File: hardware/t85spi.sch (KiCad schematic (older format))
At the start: 12 parts, among them J1 AVRISP6, P1 Ethernet, SW1 SPST, U1 ATTINY85

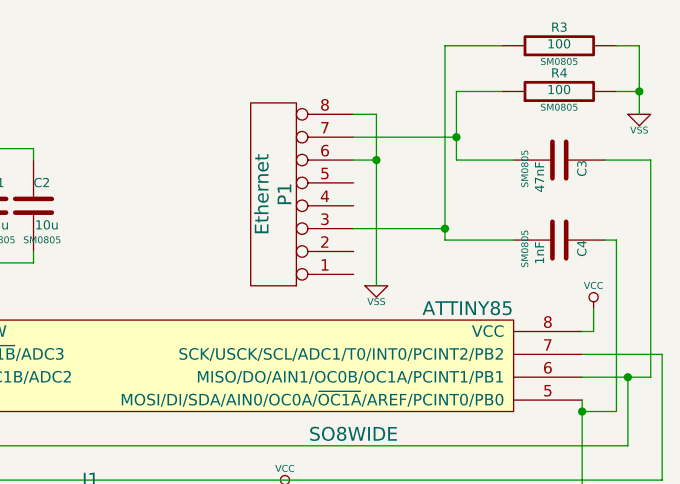
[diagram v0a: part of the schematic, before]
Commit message: fix orientation of pins
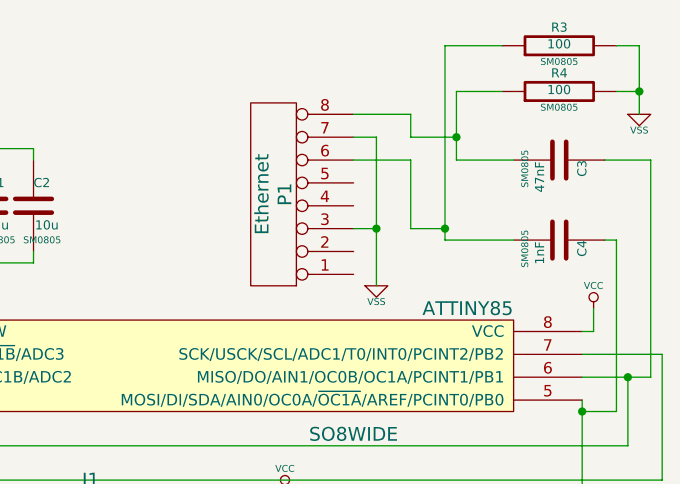
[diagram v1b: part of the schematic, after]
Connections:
- net VSS: now also P1.3 (P3), P1.7 (P7); no longer P1.6 (P6), P1.8 (P8)
- net at C3.2, R4.1: now also P1.8 (P8); no longer P1.7 (P7)
- net at C4.2, R3.1: now also P1.6 (P6); no longer P1.3 (P3)
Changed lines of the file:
@@
 Sheet 1 1
 Title ""
-Date "4 sep 2014"
+Date "5 sep 2014"
 Rev ""
 Comp ""
@@
 $EndComp
 Wire Wire Line
-	5400 1100 5400 1850
-Wire Wire Line
-	5300 1300 5400 1300
-Connection ~ 5400 1300
-Wire Wire Line
-	5300 1600 5700 1600
+	5300 1300 5550 1300
 Wire Wire Line
 	5700 800  5700 1650
@@
 	1    0    0    -1
 $EndComp
-Wire Wire Line
-	5400 1100 5300 1100
-Wire Wire Line
-	5300 1200 5750 1200
 Wire Wire Line
 	5750 1000 5750 1300
@@
 	5750 1000 5950 1000
 Connection ~ 5750 1200
+Wire Wire Line
+	5300 1100 5550 1100
+Wire Wire Line
+	5550 1100 5550 1200
+Wire Wire Line
+	5550 1200 5750 1200
+Wire Wire Line
+	5550 1300 5550 1600
+Wire Wire Line
+	5550 1600 5700 1600
+Wire Wire Line
+	5400 1200 5400 1850
+Wire Wire Line
+	5400 1600 5300 1600
+Wire Wire Line
+	5400 1200 5300 1200
+Connection ~ 5400 1600
 $EndSCHEMATC

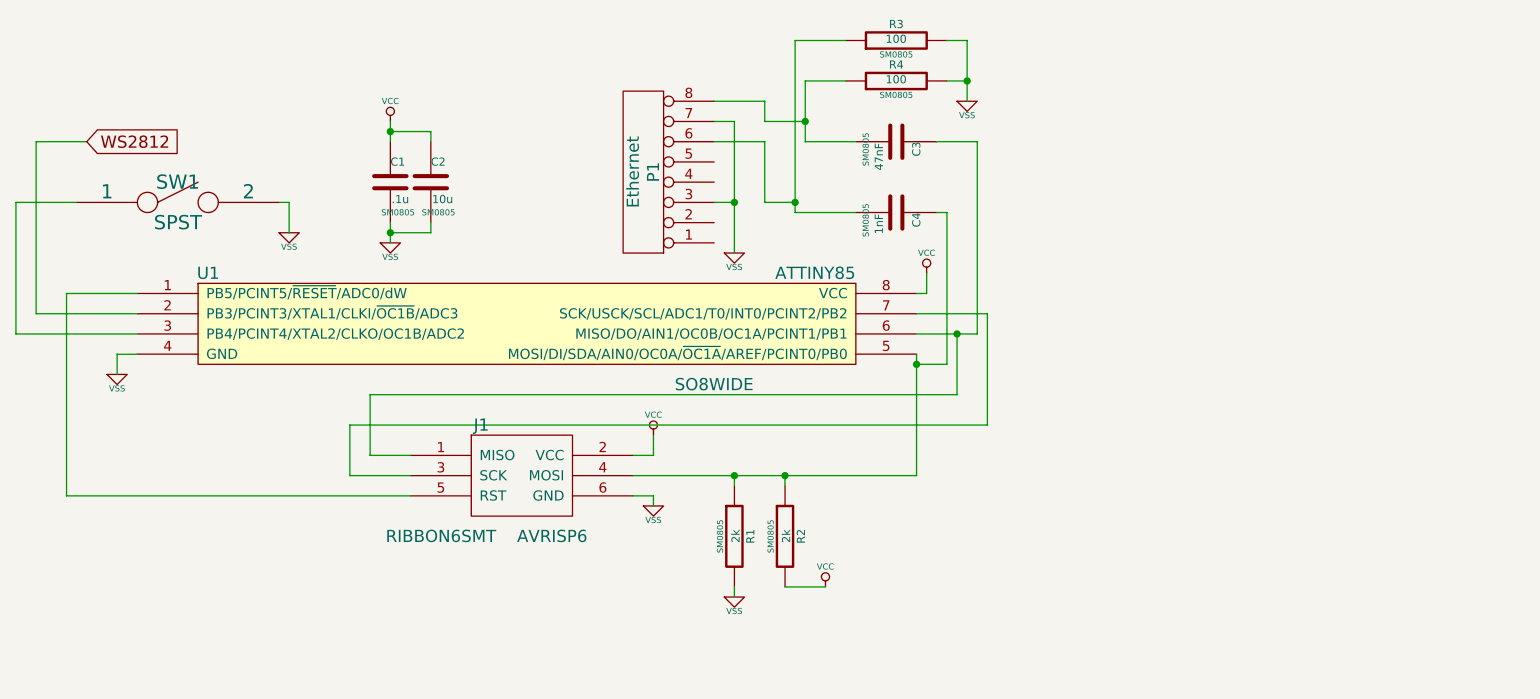
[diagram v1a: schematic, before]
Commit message: add documentation + warnings
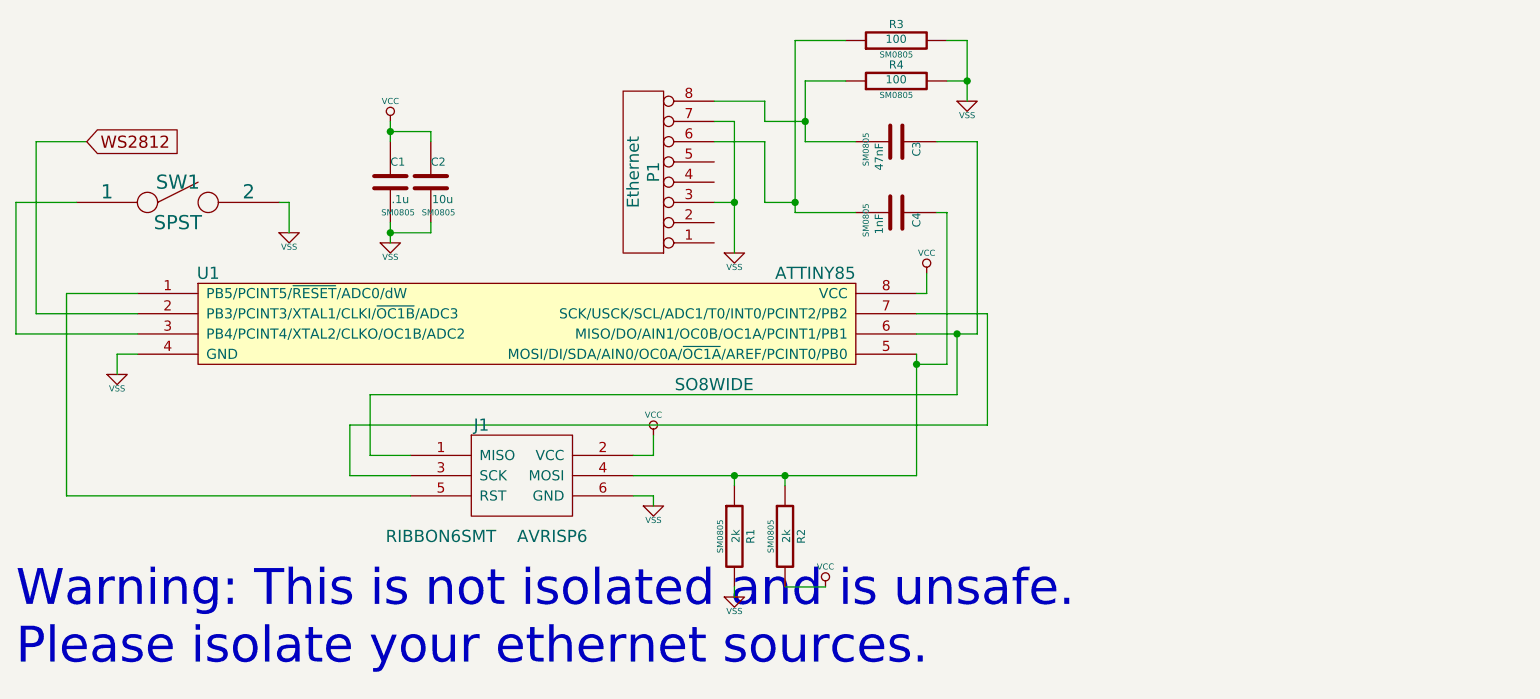
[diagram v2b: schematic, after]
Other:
- note added: "Warning: This is not isolated and is unsafe.\nPlease isolate your ethernet sources."
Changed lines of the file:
@@
 	5400 1200 5300 1200
 Connection ~ 5400 1600
+Text Notes 1850 3900 0    177  ~ 0
+Warning: This is not isolated and is unsafe.\nPlease isolate your ethernet sources.
 $EndSCHEMATC
